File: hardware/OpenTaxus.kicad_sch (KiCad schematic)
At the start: 56 parts, among them J1 OLED, J2 qwiic, J3 SWD, J4 USB_C_Receptacle_USB2.0, J5 connector, Q2 BC847BS, Q3 PT12-21B/TR8, SW1 dpad, SW2 USB_BOOT, SW3 RESET, SW4 SW_SPDT, SW5 USB_BOOT, U1 HE6206-33NR, U2 W25Q128JVS, U3 RP2040, U4 XT1861B332MR-G, Y1 YSX321SL

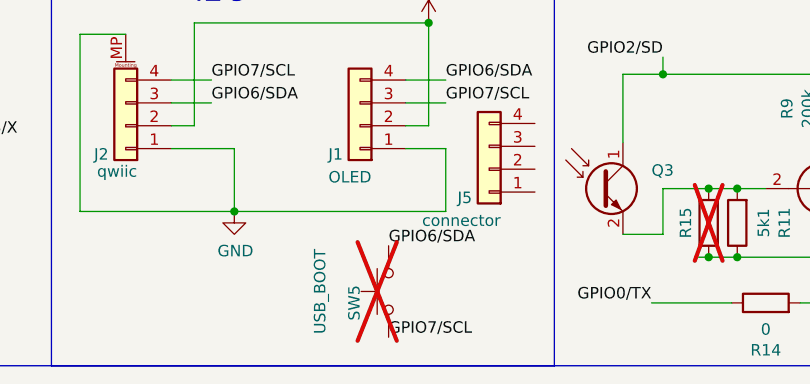
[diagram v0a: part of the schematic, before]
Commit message: remove unused i2c header
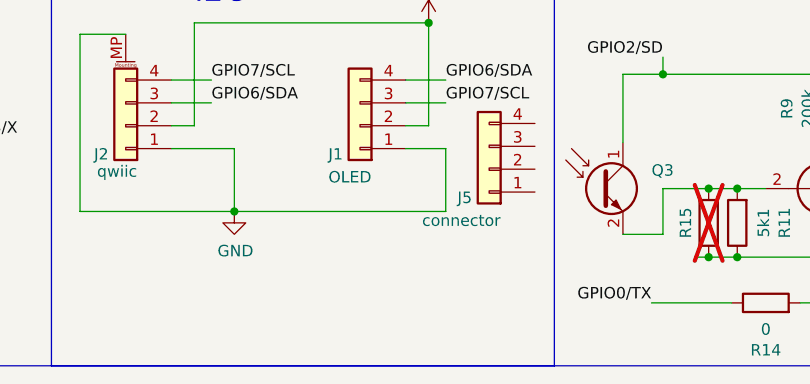
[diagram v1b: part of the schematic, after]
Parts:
- removed SW5: USB_BOOT, Jumper:SolderJumper-2_P1.3mm_Open_RoundedPad1.0x1.5mm, symbol Switch:SW_Push
- SW3: now left out of the parts list
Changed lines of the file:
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@@
 		)
 	)
-	(label "GPIO7{slash}SCL"
-		(at 100.33 194.945 0)
-		(fields_autoplaced yes)
-		(effects
-			(font
-				(size 1.27 1.27)
-			)
-			(justify left bottom)
-		)
-	)
 	(label "GPIO28_ADC2{slash}D"
 		(at 17.145 182.88 0)
@@
 		)
 	)
-	(label "GPIO6{slash}SDA"
-		(at 100.33 184.785 0)
-		(fields_autoplaced yes)
-		(effects
-			(font
-				(size 1.27 1.27)
-			)
-			(justify left bottom)
-		)
-	)
 	(label "GPIO19"
 		(at 243.84 113.665 180)
@@
 		(unit 1)
 		(exclude_from_sim no)
-		(in_bom yes)
+		(in_bom no)
 		(on_board yes)
 		(dnp yes)
@@
 					(unit 1)
 				)
-			)
-		)
-	)
-	(symbol
-		(lib_id "Switch:SW_Push")
-		(at 100.33 189.865 90)
-		(mirror x)
-		(unit 1)
-		(exclude_from_sim no)
-		(in_bom yes)
-		(on_board no)
-		(dnp yes)
-		(property "Reference" "SW5"
-			(at 96.52 191.135 0)
-			(effects
-				(font
-					(size 1.27 1.27)
-				)
-			)
-		)
-		(property "Value" "USB_BOOT"
-			(at 92.71 189.865 0)
-			(effects
-				(font
-					(size 1.27 1.27)
-				)
-			)
-		)
-		(property "Footprint" "Jumper:SolderJumper-2_P1.3mm_Open_RoundedPad1.0x1.5mm"
-			(at 95.25 189.865 0)
-			(effects
-				(font
-					(size 1.27 1.27)
-				)
-				(hide yes)
-			)
-		)
-		(property "Datasheet" "~"
-			(at 95.25 189.865 0)
-			(effects
-				(font
-					(size 1.27 1.27)
-				)
-				(hide yes)
-			)
-		)
-		(property "Description" ""
-			(at 100.33 189.865 0)
-			(effects
-				(font
-					(size 1.27 1.27)
-				)
-				(hide yes)
-			)
-		)
-		(property "LCSC" "DNP"
-			(at 100.33 189.865 0)
-			(effects
-				(font
-					(size 1.27 1.27)
-				)
-				(hide yes)
-			)
-		)
-		(property "P/N" ""
-			(at 100.33 189.865 0)
-			(effects
-				(font
-					(size 1.27 1.27)
-				)
-				(hide yes)
-			)
-		)
-		(property "Price" ""
-			(at 100.33 189.865 0)
-			(effects
-				(font
-					(size 1.27 1.27)
-				)
-				(hide yes)
-			)
-		)
-		(property "mfg" ""
-			(at 100.33 189.865 0)
-			(effects
-				(font
-					(size 1.27 1.27)
-				)
-				(hide yes)
-			)
-		)
-		(pin "1"
-		)
-		(pin "2"
-		)
-		(instances
-			(project "OpenTaxus"
-				(path "/0fe9e493-c481-454c-b8b0-96af10f6ed2d"
-					(reference "SW5")
-					(unit 1)
-				)
